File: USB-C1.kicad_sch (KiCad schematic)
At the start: 32 parts, among them J2 USB_C_Receptacle, J3 I2C_HD3SS3220, U3 HD3SS3220IRNHR, U4 TPS2068EDBVR, U5 TPD4E02B04DQA, U6 TPD4E02B04DQA, U7 TPD4E02B04DQA

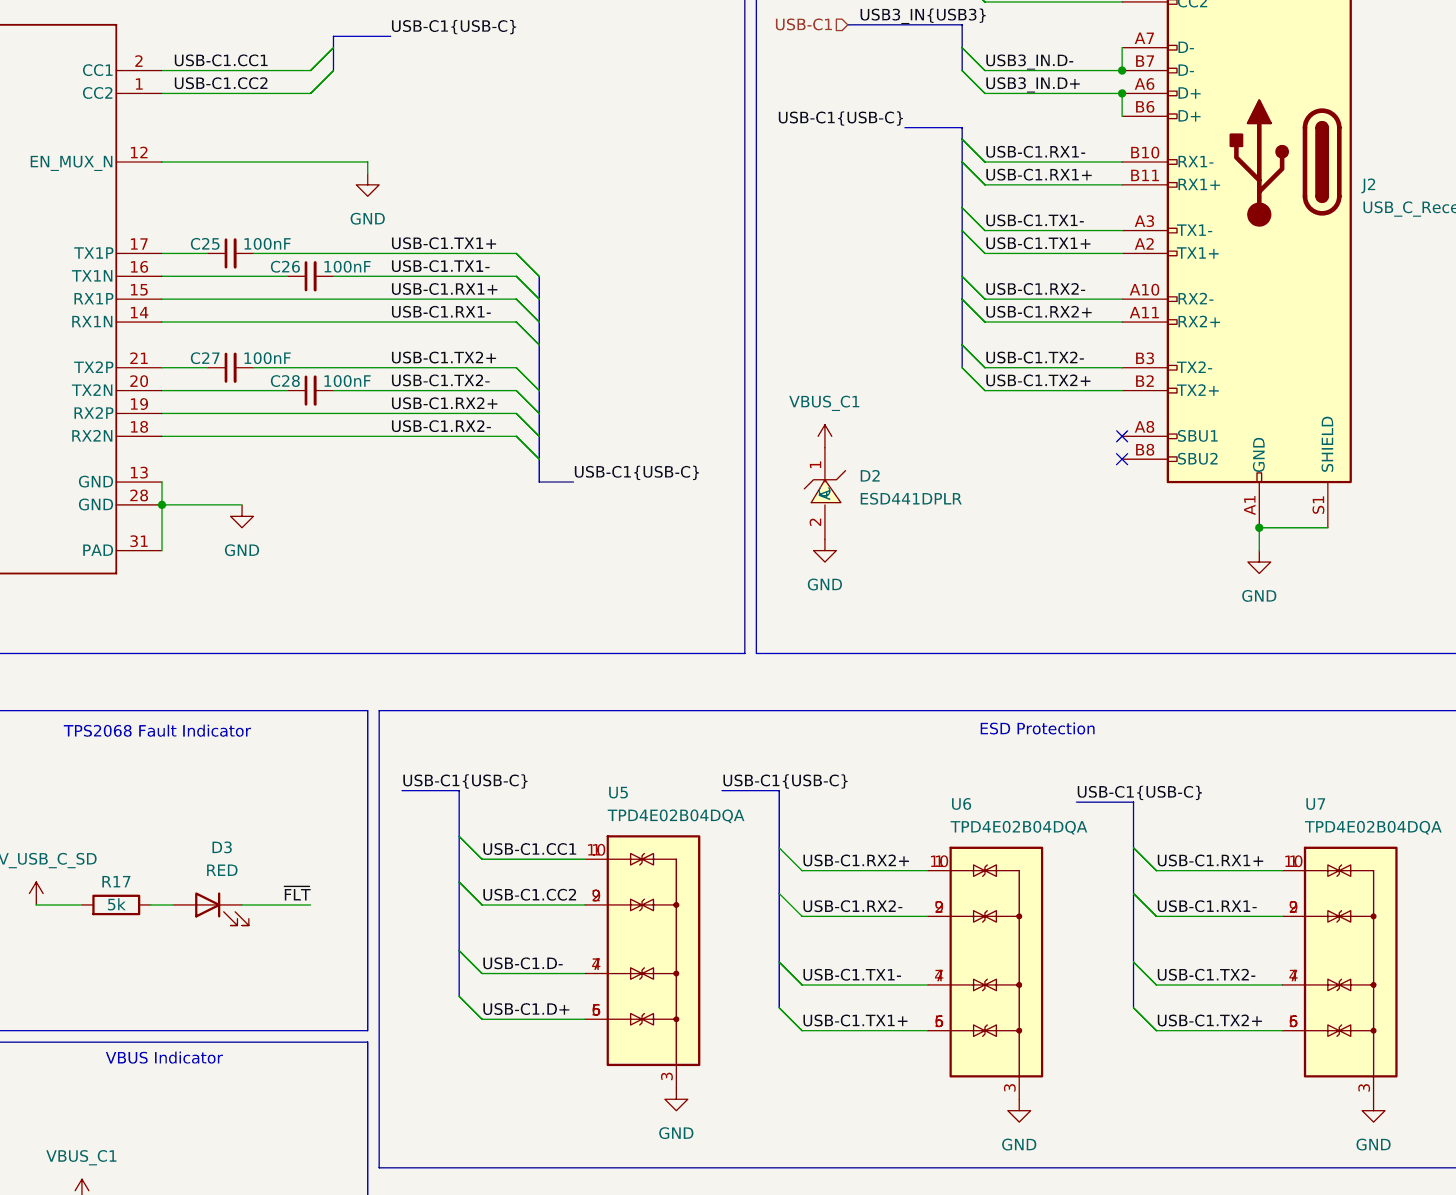
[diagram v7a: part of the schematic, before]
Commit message: minor schematic fixes, footprints changes, layout improvements
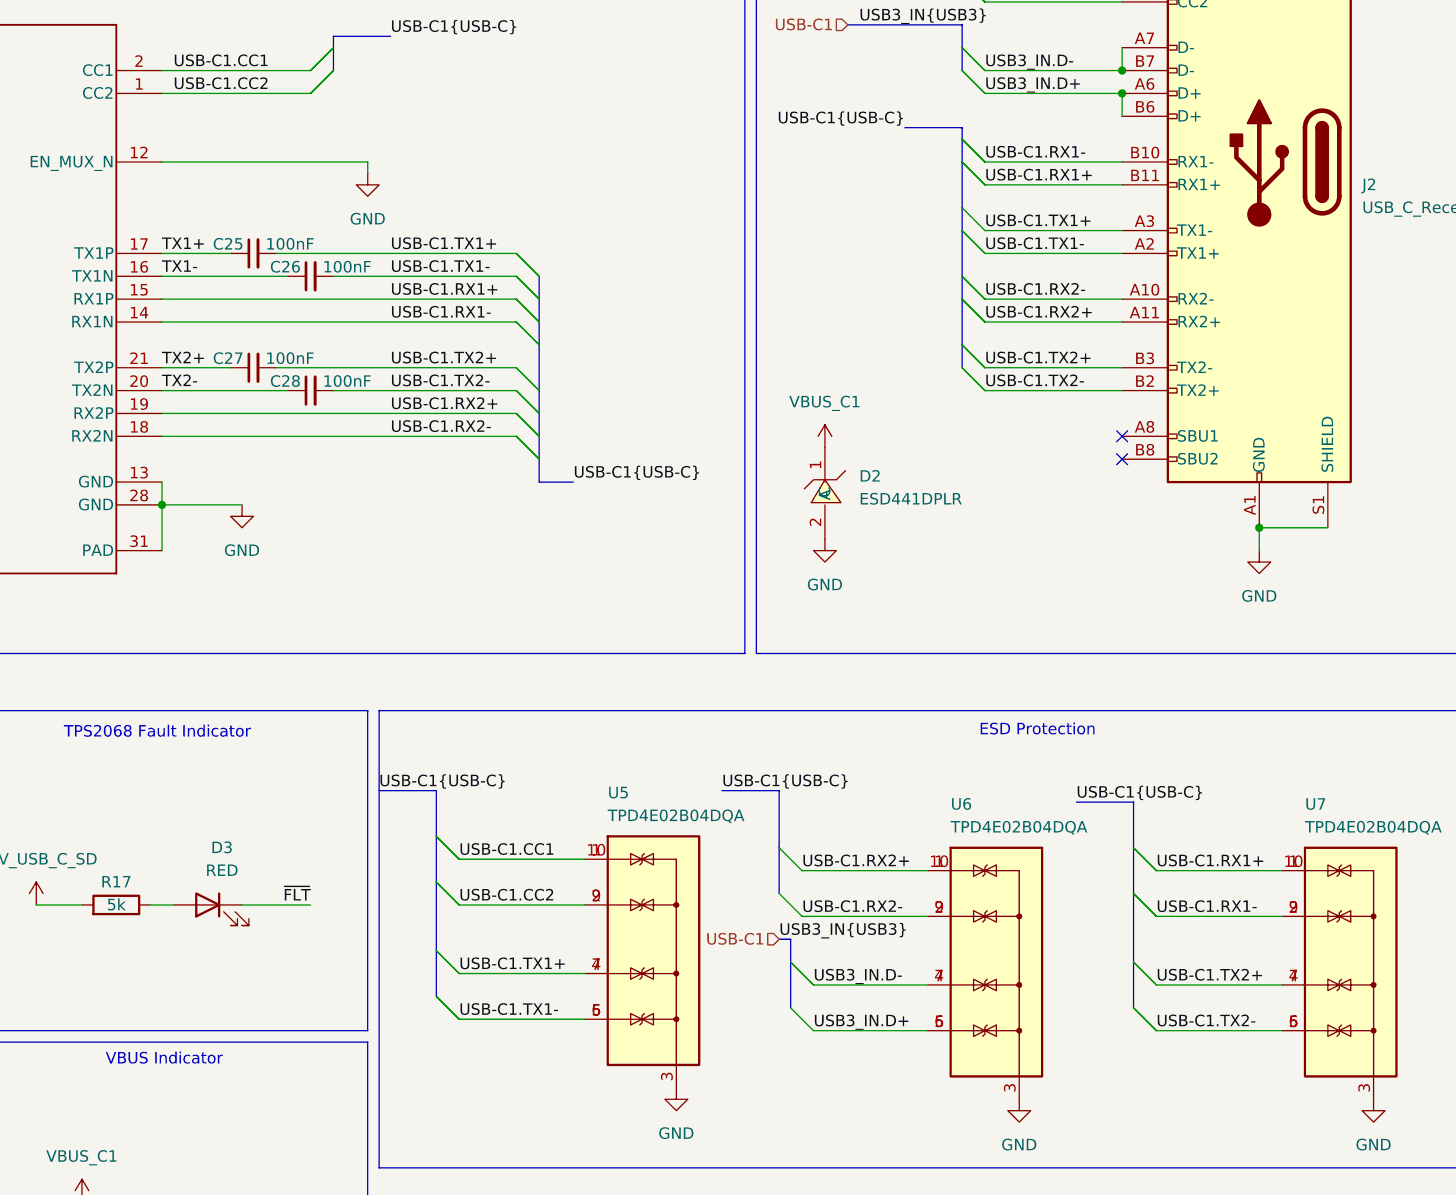
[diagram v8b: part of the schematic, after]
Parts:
- C23: footprint Capacitor_THT:C_Radial_D6.3mm_H11.0mm_P2.50mm -> Capacitor_SMD:C_0805_2012Metric; LCSC Part C109392 -> C141660
- TP1, TP2: footprint TestPoint:TestPoint_Loop_D1.80mm_Drill1.0mm_Beaded -> TestPoint:TestPoint_Pad_D1.0mm
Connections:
- net USB-C1.D+ is gone; now on net USB-C1.TX1-: U5.5 (IO4), U5.6 (NC)
- net USB-C1.D- is gone; now on net USB-C1.TX1+: U5.4 (IO3), U5.7 (NC)
- net USB-C1.TX1+: now also J2.A3 (TX1-); no longer J2.A2 (TX1+), U6.5 (IO4), U6.6 (NC)
- net USB-C1.TX1-: now also J2.A2 (TX1+); no longer J2.A3 (TX1-), U6.4 (IO3), U6.7 (NC)
- net USB-C1.TX2+: now also J2.B3 (TX2-), U7.4 (IO3), U7.7 (NC); no longer J2.B2 (TX2+), U7.5 (IO4), U7.6 (NC)
- net USB-C1.TX2-: now also J2.B2 (TX2+), U7.5 (IO4), U7.6 (NC); no longer J2.B3 (TX2-), U7.4 (IO3), U7.7 (NC)
- net USB3_IN.D+: now also U6.5 (IO4), U6.6 (NC)
- net USB3_IN.D-: now also U6.4 (IO3), U6.7 (NC)
- net TX1+: now reaches C25.1, U3.17 (TX1P)
- net TX1-: now reaches C26.1, U3.16 (TX1N)
- net TX2-: now reaches C28.1, U3.20 (TX2N)
- net TX2+: now reaches C27.1, U3.21 (TX2P)
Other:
- moved on the sheet: C25, C27
